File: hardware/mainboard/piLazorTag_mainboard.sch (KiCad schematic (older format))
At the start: 4 parts

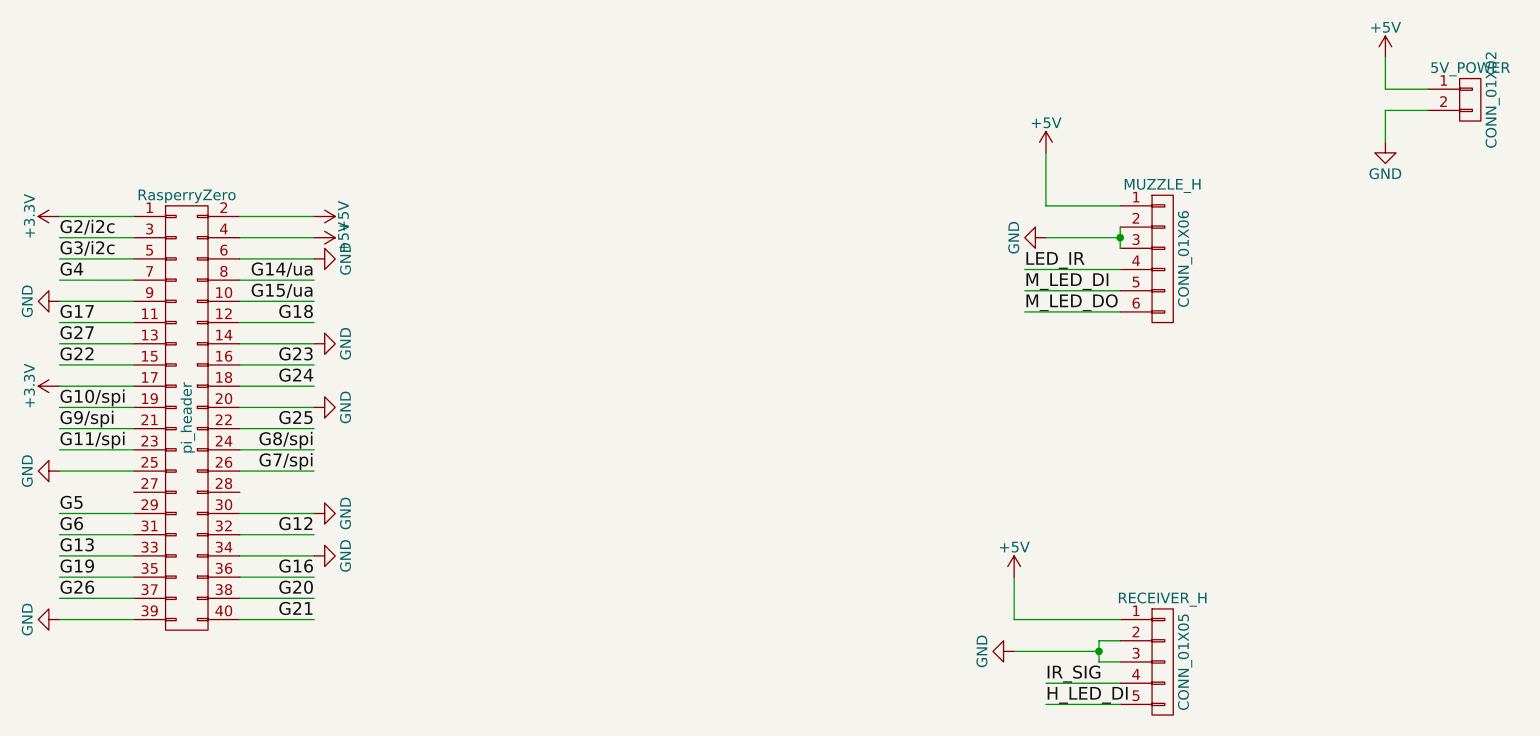
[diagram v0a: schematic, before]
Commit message: #9 New layout with pi header
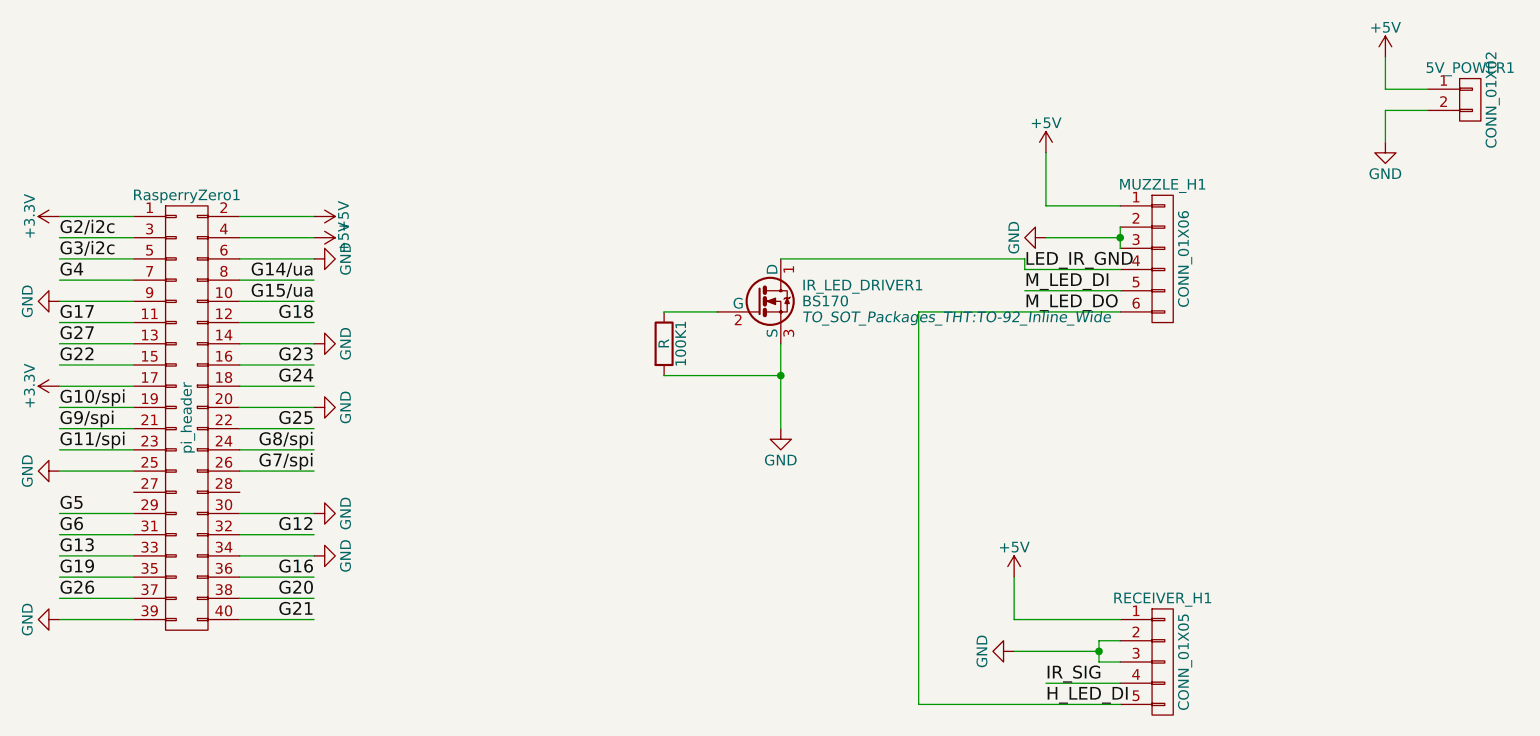
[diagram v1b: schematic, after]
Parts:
- added 100K1: R, Resistors_ThroughHole:Resistor_Horizontal_RM15mm, symbol R
- added IR_LED_DRIVER1: BS170, TO_SOT_Packages_THT:TO-92_Inline_Wide, symbol BS170
- 5V_POWER1: renamed from 5V_POWER; footprint (none) -> TO_SOT_Packages_THT:TO-92_Inline_Wide
- MUZZLE_H1: renamed from MUZZLE_H; footprint (none) -> Pin_Headers:Pin_Header_Straight_1x06
- RECEIVER_H1: renamed from RECEIVER_H; footprint (none) -> Pin_Headers:Pin_Header_Straight_1x05
- RasperryZero1: renamed from RasperryZero; footprint Pin_Headers:Pin_Header_Straight_2x20_Pitch2.54mm -> Pin_Headers:Pin_Header_Straight_2x20
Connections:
- net M_LED_DO is gone; now on net H_LED_DI: MUZZLE_H1.6 (P6)
- net GND: now also 100K1.2, IR_LED_DRIVER1.3 (S)
- net LED_IR renamed LED_IR_GND
- net LED_IR_GND: now also IR_LED_DRIVER1.1 (D)
- new net: 100K1.1, IR_LED_DRIVER1.2 (G)
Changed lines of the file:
@@
 G11/spi
 $Comp
-L pi_header RasperryZero
+L pi_header RasperryZero1
 U 1 1 58F6BD1F
 P 3800 2650
-F 0 "RasperryZero" H 3800 3700 50  0000 C CNN
+F 0 "RasperryZero1" H 3800 3700 50  0000 C CNN
 F 1 "pi_header" V 3800 2650 50  0000 C CNN
-F 2 "Pin_Headers:Pin_Header_Straight_2x20_Pitch2.54mm" H 3800 1700 50  0001 C CNN
+F 2 "Pin_Headers:Pin_Header_Straight_2x20" H 3800 1700 50  0001 C CNN
 F 3 "" H 3800 1700 50  0001 C CNN
 	1    3800 2650
@@
 	4050 3400 4400 3400
 $Comp
-L CONN_01X06 MUZZLE_H
+L CONN_01X06 MUZZLE_H1
 U 1 1 58F7073F
 P 8400 1900
-F 0 "MUZZLE_H" H 8400 2250 50  0000 C CNN
+F 0 "MUZZLE_H1" H 8400 2250 50  0000 C CNN
 F 1 "CONN_01X06" V 8500 1900 50  0000 C CNN
-F 2 "" H 8400 1900 50  0001 C CNN
+F 2 "Pin_Headers:Pin_Header_Straight_1x06" H 8400 1900 50  0001 C CNN
 F 3 "" H 8400 1900 50  0001 C CNN
 	1    8400 1900
@@
 	7850 1650 7850 1400
 $Comp
-L +5V #PWR?
+L +5V #PWR013
 U 1 1 58F708B4
 P 7850 1400
-F 0 "#PWR?" H 7850 1250 50  0001 C CNN
+F 0 "#PWR013" H 7850 1250 50  0001 C CNN
 F 1 "+5V" H 7850 1540 50  0000 C CNN
 F 2 "" H 7850 1400 50  0001 C CNN
@@
 Connection ~ 8200 1800
 $Comp
-L GND #PWR?
+L GND #PWR014
 U 1 1 58F70929
 P 7850 1800
-F 0 "#PWR?" H 7850 1550 50  0001 C CNN
+F 0 "#PWR014" H 7850 1550 50  0001 C CNN
 F 1 "GND" H 7850 1650 50  0000 C CNN
 F 2 "" H 7850 1800 50  0001 C CNN
@@
 	8200 1950 7750 1950
 Text Label 7750 1950 0    60   ~ 0
-LED_IR
+LED_IR_GND
 Wire Wire Line
 	8200 2050 7750 2050
@@
 M_LED_DI
 Wire Wire Line
-	8200 2150 7750 2150
+	7250 2150 8200 2150
 Text Label 7750 2150 0    60   ~ 0
 M_LED_DO
 $Comp
-L CONN_01X02 5V_POWER
+L CONN_01X02 5V_POWER1
 U 1 1 58F70C26
 P 9850 1150
-F 0 "5V_POWER" H 9850 1300 50  0000 C CNN
+F 0 "5V_POWER1" H 9850 1300 50  0000 C CNN
 F 1 "CONN_01X02" V 9950 1150 50  0000 C CNN
-F 2 "" H 9850 1150 50  0001 C CNN
+F 2 "TO_SOT_Packages_THT:TO-92_Inline_Wide" H 9850 1150 50  0001 C CNN
 F 3 "" H 9850 1150 50  0001 C CNN
 	1    9850 1150
@@
 	9450 1200 9450 1350
 $Comp
-L GND #PWR?
+L GND #PWR015
 U 1 1 58F70D86
 P 9450 1350
-F 0 "#PWR?" H 9450 1100 50  0001 C CNN
+F 0 "#PWR015" H 9450 1100 50  0001 C CNN
 F 1 "GND" H 9450 1200 50  0000 C CNN
 F 2 "" H 9450 1350 50  0001 C CNN
@@
 $EndComp
 $Comp
-L +5V #PWR?
+L +5V #PWR016
 U 1 1 58F70DA0
 P 9450 950
-F 0 "#PWR?" H 9450 800 50  0001 C CNN
+F 0 "#PWR016" H 9450 800 50  0001 C CNN
 F 1 "+5V" H 9450 1090 50  0000 C CNN
 F 2 "" H 9450 950 50  0001 C CNN
@@
 $EndComp
 $Comp
-L CONN_01X05 RECEIVER_H
+L CONN_01X05 RECEIVER_H1
 U 1 1 58F70948
 P 8400 3800
-F 0 "RECEIVER_H" H 8400 4100 50  0000 C CNN
+F 0 "RECEIVER_H1" H 8400 4100 50  0000 C CNN
 F 1 "CONN_01X05" V 8500 3800 50  0000 C CNN
-F 2 "" H 8400 3800 50  0001 C CNN
+F 2 "Pin_Headers:Pin_Header_Straight_1x05" H 8400 3800 50  0001 C CNN
 F 3 "" H 8400 3800 50  0001 C CNN
 	1    8400 3800
@@
 	7700 3600 7700 3400
 $Comp
-L +5V #PWR?
+L +5V #PWR017
 U 1 1 58F70A20
 P 7700 3400
-F 0 "#PWR?" H 7700 3250 50  0001 C CNN
+F 0 "#PWR017" H 7700 3250 50  0001 C CNN
 F 1 "+5V" H 7700 3540 50  0000 C CNN
 F 2 "" H 7700 3400 50  0001 C CNN
@@
 Connection ~ 8100 3750
 $Comp
-L GND #PWR?
+L GND #PWR018
 U 1 1 58F70AB7
 P 7700 3750
-F 0 "#PWR?" H 7700 3500 50  0001 C CNN
+F 0 "#PWR018" H 7700 3500 50  0001 C CNN
 F 1 "GND" H 7700 3600 50  0000 C CNN
 F 2 "" H 7700 3750 50  0001 C CNN
@@
 	7850 3900 8200 3900
 Wire Wire Line
-	8200 4000 7850 4000
+	7250 4000 8200 4000
 Text Label 7850 4000 0    60   ~ 0
 H_LED_DI
+$Comp
+L BS170 IR_LED_DRIVER1
+U 1 1 58F7369D
+P 6500 2100
+F 0 "IR_LED_DRIVER1" H 6700 2175 50  0000 L CNN
+F 1 "BS170" H 6700 2100 50  0000 L CNN
+F 2 "TO_SOT_Packages_THT:TO-92_Inline_Wide" H 6700 2025 50  0000 L CIN
+F 3 "" H 6500 2100 50  0000 L CNN
+	1    6500 2100
+	1    0    0    -1
+$EndComp
+$Comp
+L R 100K1
+U 1 1 58F737B3
+P 6050 2300
+F 0 "100K1" V 6130 2300 50  0000 C CNN
+F 1 "R" V 6050 2300 50  0000 C CNN
+F 2 "Resistors_ThroughHole:Resistor_Horizontal_RM15mm" V 5980 2300 50  0001 C CNN
+F 3 "" H 6050 2300 50  0000 C CNN
+	1    6050 2300
+	1    0    0    -1
+$EndComp
+$Comp
+L GND #PWR019
+U 1 1 58F73808
+P 6600 2700
+F 0 "#PWR019" H 6600 2450 50  0001 C CNN
+F 1 "GND" H 6600 2550 50  0000 C CNN
+F 2 "" H 6600 2700 50  0000 C CNN
+F 3 "" H 6600 2700 50  0000 C CNN
+	1    6600 2700
+	1    0    0    -1
+$EndComp
+Wire Wire Line
+	6600 2300 6600 2700
+Wire Wire Line
+	6050 2450 6600 2450
+Connection ~ 6600 2450
+Wire Wire Line
+	6050 2150 6300 2150
+Wire Wire Line
+	6600 1900 7750 1900
+Wire Wire Line
+	7750 1900 7750 1950
+Wire Wire Line
+	7250 2150 7250 4000
 $EndSCHEMATC

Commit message: #9 mainboard schemantics
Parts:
- added INPUT: CONN_01X08, symbol CONN_01X08
- added MOTOR_RUMBLE: CONN_01X02, symbol CONN_01X02
- added RUMBLE_DRIVER: L293D, DIL16, symbol L293D
- added SSD1603: CONN_01X04, symbol CONN_01X04
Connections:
- net +3V3: now also RUMBLE_DRIVER.1 (1-2EN), RUMBLE_DRIVER.16 (VCC1), SSD1603.2 (P2)
- net +5V: now also RUMBLE_DRIVER.8 (VCC2)
- net G2/i2c: now also SSD1603.4 (P4)
- net G3/i2c: now also SSD1603.3 (P3)
- net GND: now also INPUT.1 (P1), INPUT.2 (P2), RUMBLE_DRIVER.12 (GND4), RUMBLE_DRIVER.13 (GND3), RUMBLE_DRIVER.4 (GND1), RUMBLE_DRIVER.5 (GND2), RUMBLE_DRIVER.7 (2A), SSD1603.1 (P1)
- new net: MOTOR_RUMBLE.2 (P2), RUMBLE_DRIVER.3 (1Y)
- new net: MOTOR_RUMBLE.1 (P1), RUMBLE_DRIVER.6 (2Y)
- new net PI_RUMBLE: RUMBLE_DRIVER.2 (1A)

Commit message: Some minor changes on the receiver mainboard
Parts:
- added M?: LOGIC_LEVEL_CONVERTER, LOGIC_LEVEL_CONVERTER, symbol LOGIC_LEVEL_CONVERTER
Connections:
- net +3V3: now also M?.P$3 (LV)
- net +5V: now also M?.P$10 (HV)
- net GND: now also M?.P$4 (GND), M?.P$9 (GND)
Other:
- moved on the sheet: 100K1, INPUT, IR_LED_DRIVER1, MOTOR_RUMBLE, MUZZLE_H1, RECEIVER_H1, RUMBLE_DRIVER

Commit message: #9 First net generated for mainboard
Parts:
- 100K1: footprint Resistors_ThroughHole:Resistor_Horizontal_RM15mm -> Resistors_THT:R_Axial_DIN0207_L6.3mm_D2.5mm_P10.16mm_Horizontal
- 5V_POWER1: footprint TO_SOT_Packages_THT:TO-92_Inline_Wide -> Pin_Headers:Pin_Header_Straight_2x01_Pitch2.54mm
- INPUT1: renamed from INPUT; footprint (none) -> Pin_Headers:Pin_Header_Straight_1x08_Pitch2.54mm
- M1: renamed from M?; footprint LOGIC_LEVEL_CONVERTER -> SparkFun-Boards:LOGIC_LEVEL_CONVERTER
- MOTOR_RUMBLE1: renamed from MOTOR_RUMBLE; footprint (none) -> Pin_Headers:Pin_Header_Straight_1x02_Pitch2.54mm
- RECEIVER_H1: footprint Pin_Headers:Pin_Header_Straight_1x05 -> Pin_Headers:Pin_Header_Straight_1x05_Pitch2.54mm
- RUMBLE_DRIVER1: renamed from RUMBLE_DRIVER; footprint DIL16 -> L293D:DIL16
- RasperryZero1: footprint Pin_Headers:Pin_Header_Straight_2x20 -> Pin_Headers:Pin_Header_Straight_2x20_Pitch2.54mm
- SSD1603: footprint (none) -> Pin_Headers:Pin_Header_Straight_1x04_Pitch2.54mm
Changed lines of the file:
@@
 F 0 "RasperryZero1" H 3800 3700 50  0000 C CNN
 F 1 "pi_header" V 3800 2650 50  0000 C CNN
-F 2 "Pin_Headers:Pin_Header_Straight_2x20" H 3800 1700 50  0001 C CNN
+F 2 "Pin_Headers:Pin_Header_Straight_2x20_Pitch2.54mm" H 3800 1700 50  0001 C CNN
 F 3 "" H 3800 1700 50  0001 C CNN
 	1    3800 2650
@@
 F 0 "5V_POWER1" H 9850 1300 50  0000 C CNN
 F 1 "CONN_01X02" V 9950 1150 50  0000 C CNN
-F 2 "TO_SOT_Packages_THT:TO-92_Inline_Wide" H 9850 1150 50  0001 C CNN
+F 2 "Pin_Headers:Pin_Header_Straight_2x01_Pitch2.54mm" H 9850 1150 50  0001 C CNN
 F 3 "" H 9850 1150 50  0001 C CNN
 	1    9850 1150
@@
 F 0 "RECEIVER_H1" H 10650 5350 50  0000 C CNN
 F 1 "CONN_01X05" V 10750 5050 50  0000 C CNN
-F 2 "Pin_Headers:Pin_Header_Straight_1x05" H 10650 5050 50  0001 C CNN
+F 2 "Pin_Headers:Pin_Header_Straight_1x05_Pitch2.54mm" H 10650 5050 50  0001 C CNN
 F 3 "" H 10650 5050 50  0001 C CNN
 	1    10650 5050
@@
 F 0 "100K1" V 8380 3550 50  0000 C CNN
 F 1 "R" V 8300 3550 50  0000 C CNN
-F 2 "Resistors_ThroughHole:Resistor_Horizontal_RM15mm" V 8230 3550 50  0001 C CNN
+F 2 "Resistors_THT:R_Axial_DIN0207_L6.3mm_D2.5mm_P10.16mm_Horizontal" V 8230 3550 50  0001 C CNN
 F 3 "" H 8300 3550 50  0000 C CNN
 	1    8300 3550
@@
 $EndComp
 $Comp
-L L293D RUMBLE_DRIVER
+L L293D RUMBLE_DRIVER1
 U 1 1 590D950F
 P 4750 6400
-F 0 "RUMBLE_DRIVER" H 4350 7240 50  0000 L CNN
+F 0 "RUMBLE_DRIVER1" H 4350 7240 50  0000 L CNN
 F 1 "L293D" H 4350 5500 50  0000 L CNN
-F 2 "DIL16" H 4750 6400 50  0001 L CNN
+F 2 "L293D:DIL16" H 4750 6400 50  0001 L CNN
 F 3 "STMicroelectronics" H 4750 6400 50  0001 L CNN
 F 4 "Driver; 36V; Power DIP; 600mA Low LevelO/P; 1.2A O/P High Level; 4 Drivers; 7V" H 4750 6400 50  0001 L CNN "Description"
@@
 $EndComp
 $Comp
-L +3.3V #PWR?
+L +3.3V #PWR020
 U 1 1 590D9646
 P 4150 5700
-F 0 "#PWR?" H 4150 5550 50  0001 C CNN
+F 0 "#PWR020" H 4150 5550 50  0001 C CNN
 F 1 "+3.3V" H 4150 5840 50  0000 C CNN
 F 2 "" H 4150 5700 50  0001 C CNN
@@
 $EndComp
 $Comp
-L +3.3V #PWR?
+L +3.3V #PWR021
 U 1 1 590D9676
 P 5350 5700
-F 0 "#PWR?" H 5350 5550 50  0001 C CNN
+F 0 "#PWR021" H 5350 5550 50  0001 C CNN
 F 1 "+3.3V" H 5350 5840 50  0000 C CNN
 F 2 "" H 5350 5700 50  0001 C CNN
@@
 $EndComp
 $Comp
-L +5V #PWR?
+L +5V #PWR022
 U 1 1 590D9698
 P 4150 7100
-F 0 "#PWR?" H 4150 6950 50  0001 C CNN
+F 0 "#PWR022" H 4150 6950 50  0001 C CNN
 F 1 "+5V" H 4150 7240 50  0000 C CNN
 F 2 "" H 4150 7100 50  0001 C CNN
@@
 $EndComp
 $Comp
-L GND #PWR?
+L GND #PWR023
 U 1 1 590D96DD
 P 5350 6300
-F 0 "#PWR?" H 5350 6050 50  0001 C CNN
+F 0 "#PWR023" H 5350 6050 50  0001 C CNN
 F 1 "GND" H 5350 6150 50  0000 C CNN
 F 2 "" H 5350 6300 50  0001 C CNN
@@
 $EndComp
 $Comp
-L GND #PWR?
+L GND #PWR024
 U 1 1 590D96FF
 P 5350 6500
-F 0 "#PWR?" H 5350 6250 50  0001 C CNN
+F 0 "#PWR024" H 5350 6250 50  0001 C CNN
 F 1 "GND" H 5350 6350 50  0000 C CNN
 F 2 "" H 5350 6500 50  0001 C CNN
@@
 $EndComp
 $Comp
-L GND #PWR?
+L GND #PWR025
 U 1 1 590D9721
 P 4150 6300
-F 0 "#PWR?" H 4150 6050 50  0001 C CNN
+F 0 "#PWR025" H 4150 6050 50  0001 C CNN
 F 1 "GND" H 4150 6150 50  0000 C CNN
 F 2 "" H 4150 6300 50  0001 C CNN
@@
 $EndComp
 $Comp
-L GND #PWR?
+L GND #PWR026
 U 1 1 590D976C
 P 4150 6500
-F 0 "#PWR?" H 4150 6250 50  0001 C CNN
+F 0 "#PWR026" H 4150 6250 50  0001 C CNN
 F 1 "GND" H 4150 6350 50  0000 C CNN
 F 2 "" H 4150 6500 50  0001 C CNN
@@
 $EndComp
 $Comp
-L GND #PWR?
+L GND #PWR027
 U 1 1 590D9999
 P 4150 6900
-F 0 "#PWR?" H 4150 6650 50  0001 C CNN
+F 0 "#PWR027" H 4150 6650 50  0001 C CNN
 F 1 "GND" H 4150 6750 50  0000 C CNN
 F 2 "" H 4150 6900 50  0001 C CNN
@@
 PI_RUMBLE
 $Comp
-L CONN_01X02 MOTOR_RUMBLE
+L CONN_01X02 MOTOR_RUMBLE1
 U 1 1 590D9C3D
 P 3250 6400
-F 0 "MOTOR_RUMBLE" H 3250 6550 50  0000 C CNN
+F 0 "MOTOR_RUMBLE1" H 3250 6550 50  0000 C CNN
 F 1 "CONN_01X02" V 3350 6400 50  0000 C CNN
-F 2 "" H 3250 6400 50  0001 C CNN
+F 2 "Pin_Headers:Pin_Header_Straight_1x02_Pitch2.54mm" H 3250 6400 50  0001 C CNN
 F 3 "" H 3250 6400 50  0001 C CNN
 	1    3250 6400
@@
 F 0 "SSD1603" H 1900 4500 50  0000 C CNN
 F 1 "CONN_01X04" V 2000 4250 50  0000 C CNN
-F 2 "" H 1900 4250 50  0001 C CNN
+F 2 "Pin_Headers:Pin_Header_Straight_1x04_Pitch2.54mm" H 1900 4250 50  0001 C CNN
 F 3 "" H 1900 4250 50  0001 C CNN
 	1    1900 4250
@@
 $EndComp
 $Comp
-L GND #PWR?
+L GND #PWR028
 U 1 1 590DAC36
 P 1700 4100
-F 0 "#PWR?" H 1700 3850 50  0001 C CNN
+F 0 "#PWR028" H 1700 3850 50  0001 C CNN
 F 1 "GND" H 1700 3950 50  0000 C CNN
 F 2 "" H 1700 4100 50  0001 C CNN
@@
 $EndComp
 $Comp
-L +3.3V #PWR?
+L +3.3V #PWR029
 U 1 1 590DAC6E
 P 1700 4200
-F 0 "#PWR?" H 1700 4050 50  0001 C CNN
+F 0 "#PWR029" H 1700 4050 50  0001 C CNN
 F 1 "+3.3V" H 1700 4340 50  0000 C CNN
 F 2 "" H 1700 4200 50  0001 C CNN
@@
 	1200 1900 1200 4300
 $Comp
-L CONN_01X08 INPUT
+L CONN_01X08 INPUT1
 U 1 1 590DB402
 P 1900 6650
-F 0 "INPUT" H 1900 7100 50  0000 C CNN
+F 0 "INPUT1" H 1900 7100 50  0000 C CNN
 F 1 "CONN_01X08" V 2000 6650 50  0000 C CNN
-F 2 "" H 1900 6650 50  0001 C CNN
+F 2 "Pin_Headers:Pin_Header_Straight_1x08_Pitch2.54mm" H 1900 6650 50  0001 C CNN
 F 3 "" H 1900 6650 50  0001 C CNN
 	1    1900 6650
@@
 $EndComp
 $Comp
-L GND #PWR?
+L GND #PWR030
 U 1 1 590DB4A8
 P 1700 6300
-F 0 "#PWR?" H 1700 6050 50  0001 C CNN
+F 0 "#PWR030" H 1700 6050 50  0001 C CNN
 F 1 "GND" H 1700 6150 50  0000 C CNN
 F 2 "" H 1700 6300 50  0001 C CNN
@@
 $EndComp
 $Comp
-L GND #PWR?
+L GND #PWR031
 U 1 1 590DB4DA
 P 1700 6400
-F 0 "#PWR?" H 1700 6150 50  0001 C CNN
+F 0 "#PWR031" H 1700 6150 50  0001 C CNN
 F 1 "GND" H 1700 6250 50  0000 C CNN
 F 2 "" H 1700 6400 50  0001 C CNN
@@
 $EndComp
 $Comp
-L LOGIC_LEVEL_CONVERTER M?
+L LOGIC_LEVEL_CONVERTER M1
 U 1 1 590DBB7B
 P 7000 4500
-F 0 "M?" H 7000 4500 50  0001 C CNN
+F 0 "M1" H 7000 4500 50  0001 C CNN
 F 1 "LOGIC_LEVEL_CONVERTER" H 7000 4500 50  0001 C CNN
-F 2 "LOGIC_LEVEL_CONVERTER" H 7030 4650 20  0001 C CNN
+F 2 "SparkFun-Boards:LOGIC_LEVEL_CONVERTER" H 7030 4650 20  0001 C CNN
 F 3 "" H 7000 4500 60  0001 C CNN
 	1    7000 4500
@@
 $EndComp
 $Comp
-L GND #PWR?
+L GND #PWR032
 U 1 1 590DBD15
 P 5800 3600
-F 0 "#PWR?" H 5800 3350 50  0001 C CNN
+F 0 "#PWR032" H 5800 3350 50  0001 C CNN
 F 1 "GND" H 5800 3450 50  0000 C CNN
 F 2 "" H 5800 3600 50  0001 C CNN
@@
 $EndComp
 $Comp
-L GND #PWR?
+L GND #PWR033
 U 1 1 590DBD3D
 P 7300 3600
-F 0 "#PWR?" H 7300 3350 50  0001 C CNN
+F 0 "#PWR033" H 7300 3350 50  0001 C CNN
 F 1 "GND" H 7300 3450 50  0000 C CNN
 F 2 "" H 7300 3600 50  0001 C CNN
@@
 $EndComp
 $Comp
-L +5V #PWR?
+L +5V #PWR034
 U 1 1 590DBD65
 P 7300 3500
-F 0 "#PWR?" H 7300 3350 50  0001 C CNN
+F 0 "#PWR034" H 7300 3350 50  0001 C CNN
 F 1 "+5V" H 7300 3640 50  0000 C CNN
 F 2 "" H 7300 3500 50  0001 C CNN
@@
 $EndComp
 $Comp
-L +3.3V #PWR?
+L +3.3V #PWR035
 U 1 1 590DBD8D
 P 5800 3500
-F 0 "#PWR?" H 5800 3350 50  0001 C CNN
+F 0 "#PWR035" H 5800 3350 50  0001 C CNN
 F 1 "+3.3V" H 5800 3640 50  0000 C CNN
 F 2 "" H 5800 3500 50  0001 C CNN
